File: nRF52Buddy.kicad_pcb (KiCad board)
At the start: 4 copper layers, 60 x 35 mm, 98 parts, among them J1 2060-452_998-404, J2 SWD, J3 2305018-2, J4 Conn_02x26_Odd_Even, J5 Conn_02x26_Odd_Even, J6 S2B-PH-SM4-TB(LF)(SN), Q1 SSM3J332R, Q2 SSM3J332R, Q3 SSM3J332R, Q4 SSM3J332R, SW1 SW_SPST, U1 AP9211, U2 MAX17260SETD, U3 TP4054, U4 TP6841S6, U5 MIC5205-3.3YM5, U6 MDBT50Q-1MV2, U7 USBLC6-2SC6, Y1 32.768 kHz

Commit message: Updates for revision 2
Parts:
- removed NT7: NetTie_2, Footprints:NetTie-2_SMD_Pad0.15mm
- removed Q4: SSM3J332R, Package_TO_SOT_SMD:SOT-23
- removed R23, R24, R25, R30: 10k, Resistor_SMD:R_0402_1005Metric
- added D14: D_Small, Diode_SMD:D_SOD-123F, F.Cu at (118.2, 115.8)
- added D15: D_Small, Diode_SMD:D_SOD-123F, F.Cu at (113.9, 121.4)
- J1: footprint SnapEDA Library:WAGO_2060-452_998-404 -> Footprints:WAGO_2060-452_998-404
- J3: footprint SnapEDA Library:TE_2305018-2 -> Footprints:TE_2305018-2
- J6: value S2B-PH-SM4-TB(LF)(SN) -> HDGC1251WR-S-2P; footprint Footprints:JST_S2B-PH-SM4-TB(LF)(SN) -> Footprints:HDGC1251WR-S-2P
- R32: value 10k -> 1k5
- R7: value 10 -> 10R
- SW1: footprint myFootprints:TS-1089S-02526 -> Footprints:TS-1089S-02526
- moved D16 20.1 mm to (112.8, 109.7)
- moved C14 18.7 mm to (98.4, 122.1)
- moved U5 18.7 mm to (98.4, 119.5)
- moved C13 18.0 mm to (99.6, 116.4)
- moved C11 17.8 mm to (97.6, 116.9)
- moved C12 17.8 mm to (97.6, 115.9)
- moved R32 15.6 mm to (104.7, 110.6), turned to -90 degrees
- moved D12 14.9 mm to (112.8, 107.7), turned to 0 degrees
- moved R21 11.0 mm to (115.0, 107.7)
- moved R1 8.86 mm to (89.4, 125.5), turned to 0 degrees
- moved D1 8.71 mm to (103.1, 120.0), turned to 90 degrees
- moved R5 8.21 mm to (121.9, 116.1), turned to -90 degrees
- moved R3 7.23 mm to (120.9, 116.1), turned to 90 degrees
- moved J6 6.33 mm to (83.3, 124.0), turned to 180 degrees
- moved U1 6.11 mm to (89.1, 123.1), turned to -90 degrees
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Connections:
- C19 pad 2: VCC -> +3V3
- C20 pad 2: VCC -> +3V3
- C3 pad 1: /Power Input/BATT_IN -> /Power Input/BATT_CONN+
- C4 pad 1: VCC -> /Power Input/BATT_CONN+
- C6 pad 1: /Power Input/+12V -> /Power Switching/12V_REG_IN
- C7 pad 1: /Power Input/+12V -> /Power Switching/12V_REG_IN
- D1 pad 1: GND -> /Power Input/+12V_CONN
- D1 pad 2: /Power Input/+12V_CONN -> GND
- D16 pad 1: /Power Input/~{CHARGE} -> /P1.09/~{CHARGE}
- D2 pad 1: VCC -> +3V3
- J2 pad 1: VCC -> +3V3
- J4 pad 48: /Connectors/P1.09 -> /P1.09/~{CHARGE}
- J4 pad 51: VCC -> +3V3
- J4 pad 52: VCC -> +3V3
- L3 pad 2: VCC -> +3V3
- R19 pad 2: VCC -> +3V3
- R2 pad 2: /Power Input/BATT_IN -> /Power Input/BATT_CONN+
- R20 pad 2: VCC -> +3V3
- R32 pad 2: +5V -> +3V3
- U1 pad 3: VCC -> /Power Input/BATT_CONN+
- U2 pad 6: /Power Input/BATT_IN -> /Power Input/BATT_CONN+
- U2 pad 7: /Power Input/BATT_IN -> /Power Input/BATT_CONN+
- U3 pad 1: /Power Input/~{CHARGE} -> /P1.09/~{CHARGE}
- U3 pad 3: /Power Input/BATT_CONN+ -> /Power Input/BATT+
- U4 pad 4: /Power Switching/12V EN -> /Power Switching/12V_REG_IN
- U4 pad 5: /Power Input/+12V -> /Power Switching/12V_REG_IN
- U5 pad 3: /Power Switching/3V3_EN -> VCC
- U6 pad 26: /Connectors/P1.09 -> /P1.09/~{CHARGE}
- U6 pad 28: VCC -> +3V3
- U6 pad 30: VCC -> +3V3
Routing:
- net +3V3: track 27.5 -> 137.5 mm, vias 1 -> 5
- net VCC: track 119.5 -> 9.57 mm, vias 5 -> 0
- net /P1.09/~{CHARGE}: track 0.00 -> 48.3 mm, vias 0 -> 4
- net /Connectors/P1.09: track 23.0 -> 0.00 mm, vias 2 -> 0
- net /Power Input/~{CHARGE}: track 20.6 -> 0.00 mm, vias 3 -> 0
- net /Power Input/+12V_CONN: track 8.44 -> 28.5 mm
- net /Power Switching/V_USB_FILT: track 50.6 -> 36.7 mm
- net +5V: track 35.3 -> 48.8 mm, vias 2 -> 4
- net /Power Input/BATT+: track 3.96 -> 15.2 mm
- net Net-(D16-A): track 1.57 -> 11.8 mm, vias 0 -> 2
- net GND: track 66.9 -> 76.7 mm, vias 318 -> 260
- net /Power Switching/12V__GATE_EN: track 13.9 -> 5.15 mm
- net /Power Input/+12V: track 18.5 -> 10.1 mm
- net /Power Input/BATT_CONN-: track 0.00 -> 7.65 mm
- net /Power Switching/12V_REG_IN: track 0.00 -> 7.29 mm
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- added copper zone on F.Cu, net /Power Input/BATT_CONN+
- added copper zone on F.Cu, net /Power Switching/12V_REG_IN
- removed copper zone on F.Cu, net /Power Input/+12V
- removed copper zone on F.Cu, net /Power Input/BATT+
- removed copper zone on F.Cu, net /Power Input/BATT_IN
- removed copper zone on F.Cu, net /Power Switching/V_USB
- removed copper zone on F.Cu, net /Power Switching/V_USB_FILT
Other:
- board text added: "+12V"
- board text added: "BATT+"
- board text added: "BATT-"
- board text added: "GND"
- board text added: "KS 04/23"
- board text added: "RESET"
- board text removed: "+"
- board text removed: "-"
- board text removed: "12V EN"
- board text removed: "KS 11/22"
- board text removed: "RST"

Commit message: updating bom
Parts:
- D1: value D_TVS -> D_TVS_15V
- D2, D3, D4, D5, D6: value D_TVS -> D_TVS_5V

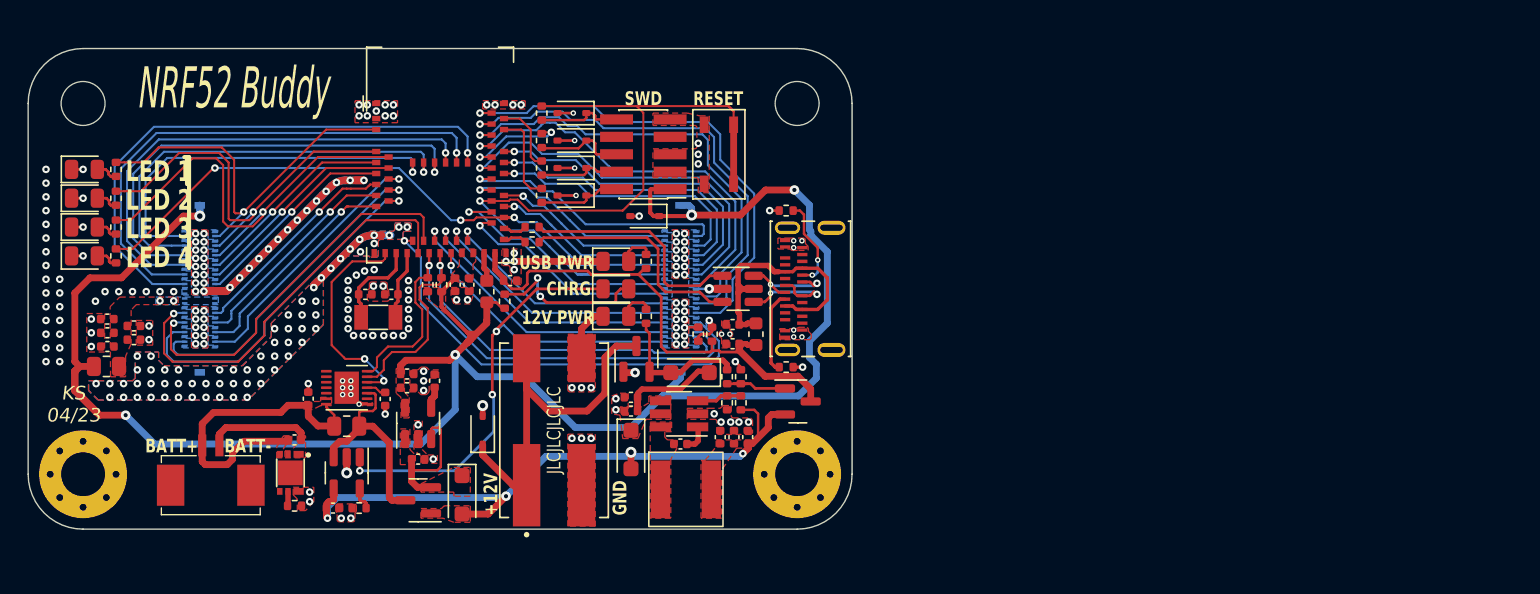
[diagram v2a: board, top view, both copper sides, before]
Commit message: Removing all traces. All components exclusing LEDs, connectors, BLE module, and switching power supply have been placed off of board
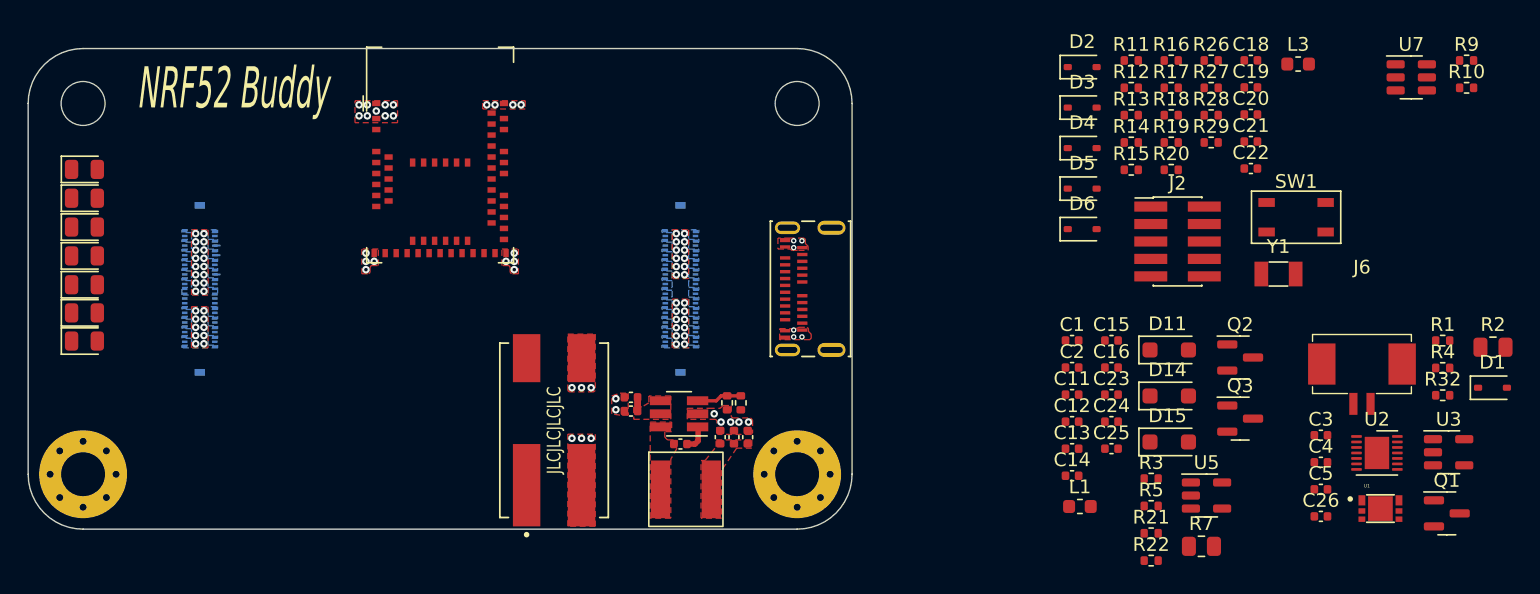
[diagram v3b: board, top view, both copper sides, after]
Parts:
- U1: footprint AP9211SA-AK-HAC-7:DFN200X300X60-7N -> Footprints:DFN200X300X60-7N
- moved R1 84.5 mm to (173.0, 113.5)
- moved J6 84.3 mm to (167.1, 115.2), turned to 0 degrees
- moved R2 83.7 mm to (176.7, 114.0), turned to 0 degrees
- moved R7 80.8 mm to (155.4, 128.4), turned to 0 degrees
- moved U3 80.3 mm to (173.4, 121.6), turned to 0 degrees
- moved R4 79.6 mm to (173.0, 115.5)
- moved U1 79.4 mm to (168.5, 125.7), turned to 0 degrees
- moved R18 77.3 mm to (153.2, 97.0), turned to 0 degrees
- moved U2 75.2 mm to (168.2, 121.7)
- moved R12 74.9 mm to (150.3, 95.1), turned to 0 degrees
- moved C4 74.8 mm to (164.1, 122.3)
- moved R11 74.4 mm to (150.3, 93.1), turned to 0 degrees
- moved R14 74.0 mm to (150.3, 99.0), turned to 0 degrees
- moved C3 73.8 mm to (164.1, 120.4), turned to 0 degrees
- moved C25 73.7 mm to (148.9, 121.3), turned to 0 degrees
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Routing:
- net +3V3: track 137.5 -> 0.00 mm, vias 5 -> 0
- net GND: track 76.7 -> 0.00 mm, vias 260 -> 90
- net /MCU (nRF52840)/P0.18/~{NRF_RESET}: track 56.4 -> 0.00 mm, vias 1 -> 0
- net +5V: track 48.8 -> 0.00 mm, vias 4 -> 0
- net /P1.09/~{CHARGE}: track 48.3 -> 0.00 mm, vias 4 -> 0
- net /MCU (nRF52840)/P0.13/BT_STATUS_LED: track 47.3 -> 0.00 mm, vias 3 -> 0
- net /Connectors/P1.01: track 41.2 -> 0.00 mm, vias 1 -> 0
- net /SCL: track 40.0 -> 0.00 mm, vias 1 -> 0
- net /SDA: track 38.7 -> 0.00 mm, vias 1 -> 0
- net /Connectors/P1.03: track 38.5 -> 0.00 mm, vias 1 -> 0
- net /Power Switching/V_USB_FILT: track 36.7 -> 0.00 mm
- net /Connectors/P0.10/NFC2: track 36.3 -> 0.00 mm, vias 1 -> 0
- net /Connectors/P0.26: track 35.9 -> 0.00 mm, vias 2 -> 0
- net /Connectors/P1.05: track 35.7 -> 0.00 mm, vias 1 -> 0
- net /Connectors/P0.09/NFC1: track 34.8 -> 0.00 mm, vias 1 -> 0
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- removed copper zone on F.Cu, net +3V3
- removed copper zone on F.Cu, net /Power Input/BATT_CONN+
- removed copper zone on F.Cu, net /Power Input/BATT_CONN-
- removed copper zone on B.Cu, net 3V3A
- removed copper zone on F.Cu, net 3V3A
- removed copper zone on In1.Cu, net GND
- removed copper zone on In2.Cu, net GND
- removed copper zone on F.Cu, net VCC
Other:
- board text removed: "+12V"
- board text removed: "12V PWR"
- board text removed: "BATT+"
- board text removed: "BATT-"
- board text removed: "CHRG"
- board text removed: "GND"
- board text removed: "KS 04/23"
- board text removed: "LED 1"
- board text removed: "LED 2"
- board text removed: "LED 3"
- board text removed: "LED 4"
- board text removed: "RESET"
- board text removed: "SWD"
- board text removed: "USB PWR"
